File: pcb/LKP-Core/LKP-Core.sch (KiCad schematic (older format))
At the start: 30 parts, among them J1 Intercon L, J2 Intercon R, J3 Power JST XH, J4 IO, J5 SWD, U1 CY8C4246AZI-M445

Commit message: Initial placement plan
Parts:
- C1, C10, C4, C6: footprint (none) -> Capacitor_SMD:C_0603_1608Metric; Comments (none) -> Jellybean part. X5R or better.; Part Number (none) -> CL10B104KA8NNNC
- C11, C2, C3, C5, C8: footprint (none) -> Capacitor_SMD:C_0603_1608Metric; Comments (none) -> Jellybean part. X5R or better.; Part Number (none) -> CC0603KRX5R8BB105
- C7: value 10nF -> 10nF C0G; footprint (none) -> Capacitor_SMD:C_0805_2012Metric; Manufacturer (none) -> Murata Electronics; Part Number (none) -> GRM2195C1H103JA01D; Supplier (none) -> lcsc:C97905
- C9: value 2.2nF -> 2.2nF C0G; footprint (none) -> Capacitor_SMD:C_0603_1608Metric; Manufacturer (none) -> Murata Electronics; Part Number (none) -> GCM1885C1H222JA16D; Supplier (none) -> lcsc:C343869
- D1: value LED -> Yellow; footprint (none) -> LED_SMD:LED_0805_2012Metric
- D2: footprint (none) -> Diode_SMD:D_SOD-123; Part Number (none) -> MBR0520L
- FB1: footprint (none) -> Inductor_SMD:L_0603_1608Metric
- J1, J2: footprint (none) -> Connector_PinSocket_2.54mm:PinSocket_2x09_P2.54mm_Vertical_SMD
- J3: value Power JST XH -> Power JST PH; footprint (none) -> Connector_JST:JST_PH_S2B-PH-SM4-TB_1x02-1MP_P2.00mm_Horizontal; Comments (none) -> Jellybean part.
- J4: footprint (none) -> Connector_PinHeader_2.54mm:PinHeader_1x06_P2.54mm_Vertical
- J5: footprint (none) -> Connector_PinHeader_2.54mm:PinHeader_1x05_P2.54mm_Vertical
- R1, R2: footprint (none) -> Resistor_SMD:R_0603_1608Metric
- RN1: footprint (none) -> Resistor_SMD:R_Array_Convex_4x0402; Manufacturer (none) -> Uniroyal; Part Number (none) -> 4D02WGJ0561TCE; Supplier (none) -> lcsc:C270386
- RN2, RN3, RN4, RN5, RN6, RN7, RN8: footprint (none) -> Resistor_SMD:R_Array_Convex_4x0402; Part Number (none) -> 4D02WGJ0561TCE
- U1: Part Number (none) -> CY8C4246AZI-M445
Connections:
- wire segments 171 -> 176
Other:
- moved on the sheet: C9, D2, FB1

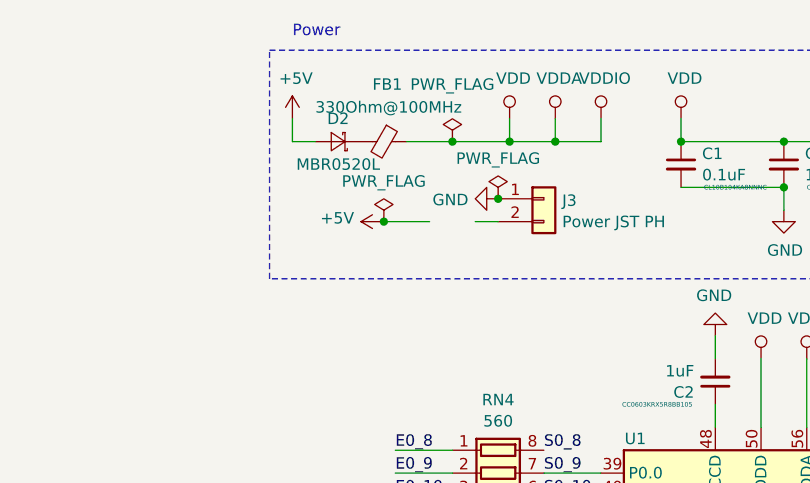
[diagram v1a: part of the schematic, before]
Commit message: Define net classes
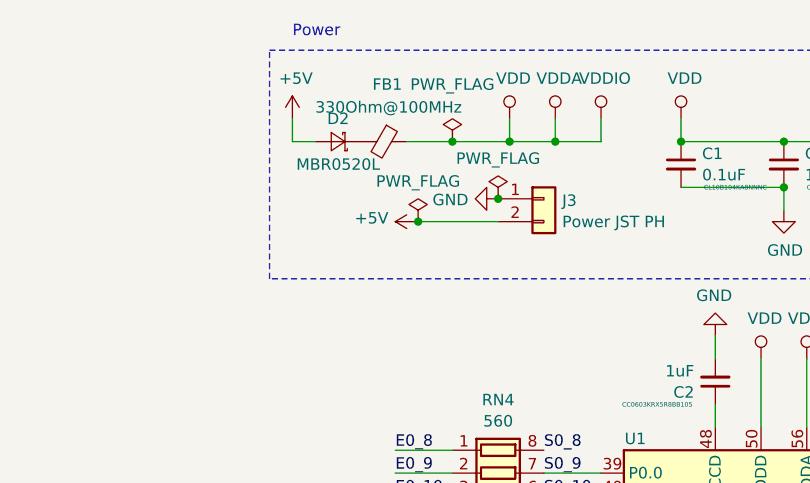
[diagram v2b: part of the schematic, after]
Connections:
- wire segments 176 -> 175
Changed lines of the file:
@@
 L power:+5V #PWR02
 U 1 1 5D5A13B9
-P 3900 1400
-F 0 "#PWR02" H 3900 1250 50  0001 C CNN
-F 1 "+5V" V 3915 1530 50  0000 L CNN
-F 2 "" H 3900 1400 50  0001 C CNN
-F 3 "" H 3900 1400 50  0001 C CNN
-	1    3900 1400
+P 4050 1400
+F 0 "#PWR02" H 4050 1250 50  0001 C CNN
+F 1 "+5V" V 4065 1530 50  0000 L CNN
+F 2 "" H 4050 1400 50  0001 C CNN
+F 3 "" H 4050 1400 50  0001 C CNN
+	1    4050 1400
 	0    -1   -1   0
 $EndComp
@@
 L power:PWR_FLAG #FLG01
 U 1 1 5D770DDD
-P 3900 1400
-F 0 "#FLG01" H 3900 1475 50  0001 C CNN
-F 1 "PWR_FLAG" H 3900 1576 50  0000 C CNN
-F 2 "" H 3900 1400 50  0001 C CNN
-F 3 "~" H 3900 1400 50  0001 C CNN
-	1    3900 1400
+P 4050 1400
+F 0 "#FLG01" H 4050 1475 50  0001 C CNN
+F 1 "PWR_FLAG" H 4050 1576 50  0000 C CNN
+F 2 "" H 4050 1400 50  0001 C CNN
+F 3 "~" H 4050 1400 50  0001 C CNN
+	1    4050 1400
 	1    0    0    -1
 $EndComp
@@
 	-1   0    0    1
 $EndComp
-Wire Wire Line
-	4400 1400 4300 1400
-Connection ~ 3900 1400
-Wire Wire Line
-	3900 1400 4100 1400
 Wire Wire Line
 	6450 3600 7700 3600
@@
 Wire Wire Line
 	3600 1050 3500 1050
+Wire Wire Line
+	4400 1400 4050 1400
+Connection ~ 4050 1400
 $EndSCHEMATC

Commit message: Finishing up
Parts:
- removed D1: Yellow, LED_SMD:LED_0805_2012Metric, symbol Device:LED
- removed R1: 1k, Resistor_SMD:R_0603_1608Metric, symbol Device:R_Small
- renumbered D2 to D1
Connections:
- net labels removed: LED_STAT
- wire segments 175 -> 172
- no-connect marks 8 -> 9
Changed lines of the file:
@@
 Text Label 7200 2600 2    50   ~ 0
 LED
-Text Label 4450 4000 0    50   ~ 0
-LED_STAT
 Wire Wire Line
 	6700 3200 6450 3200
@@
 Wire Wire Line
 	4000 3100 4850 3100
-$Comp
-L Device:LED D1
-U 1 1 5D6D02DC
-P 3700 4150
-F 0 "D1" H 3693 4369 50  0000 C CNN
-F 1 "Yellow" H 3693 4276 50  0000 C CNN
-F 2 "LED_SMD:LED_0805_2012Metric" H 3700 4150 50  0001 C CNN
-F 3 "~" H 3700 4150 50  0001 C CNN
-	1    3700 4150
-	1    0    0    -1
-$EndComp
-Wire Wire Line
-	4200 4000 4200 4150
-Wire Wire Line
-	4200 4000 4850 4000
-$Comp
-L power:GND #PWR01
-U 1 1 5D6DFC49
-P 3550 4150
-F 0 "#PWR01" H 3550 3900 50  0001 C CNN
-F 1 "GND" V 3555 4020 50  0000 R CNN
-F 2 "" H 3550 4150 50  0001 C CNN
-F 3 "" H 3550 4150 50  0001 C CNN
-	1    3550 4150
-	0    1    1    0
-$EndComp
-$Comp
-L Device:R_Small R1
-U 1 1 5D6ECD34
-P 3950 4150
-F 0 "R1" V 3751 4150 50  0000 C CNN
-F 1 "1k" V 3844 4150 50  0000 C CNN
-F 2 "Resistor_SMD:R_0603_1608Metric" H 3950 4150 50  0001 C CNN
-F 3 "~" H 3950 4150 50  0001 C CNN
-	1    3950 4150
-	0    1    1    0
-$EndComp
-Wire Wire Line
-	4050 4150 4200 4150
 Wire Wire Line
 	3500 950  3500 1050
@@
 Sensor Interconnects
 Wire Notes Line
-	8200 3350 10050 3350
-Wire Notes Line
 	10050 3350 10050 4150
 Wire Notes Line
@@
 I/O
 $Comp
-L Device:D_Schottky_Small D2
+L Device:D_Schottky_Small D1
 U 1 1 5D93FA0B
 P 3700 1050
-F 0 "D2" H 3700 950 50  0000 C CNN
+F 0 "D1" H 3700 950 50  0000 C CNN
 F 1 "MBR0520L" H 3700 1150 50  0000 C CNN
 F 2 "Diode_SMD:D_SOD-123" V 3700 1050 50  0001 C CNN
@@
 	4400 1400 4050 1400
 Connection ~ 4050 1400
+NoConn ~ 4850 4000
 $EndSCHEMATC

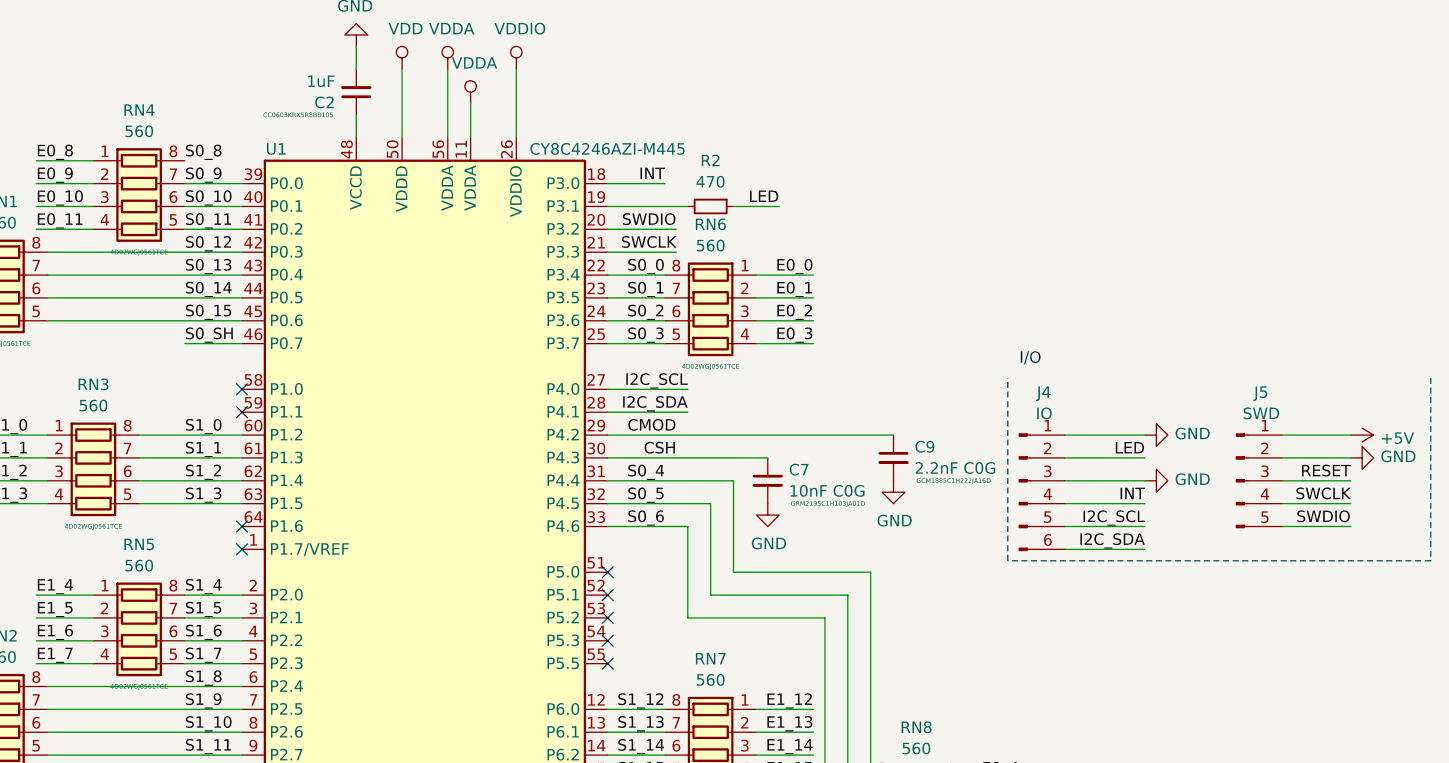
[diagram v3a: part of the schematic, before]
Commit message: Move various IO pins down
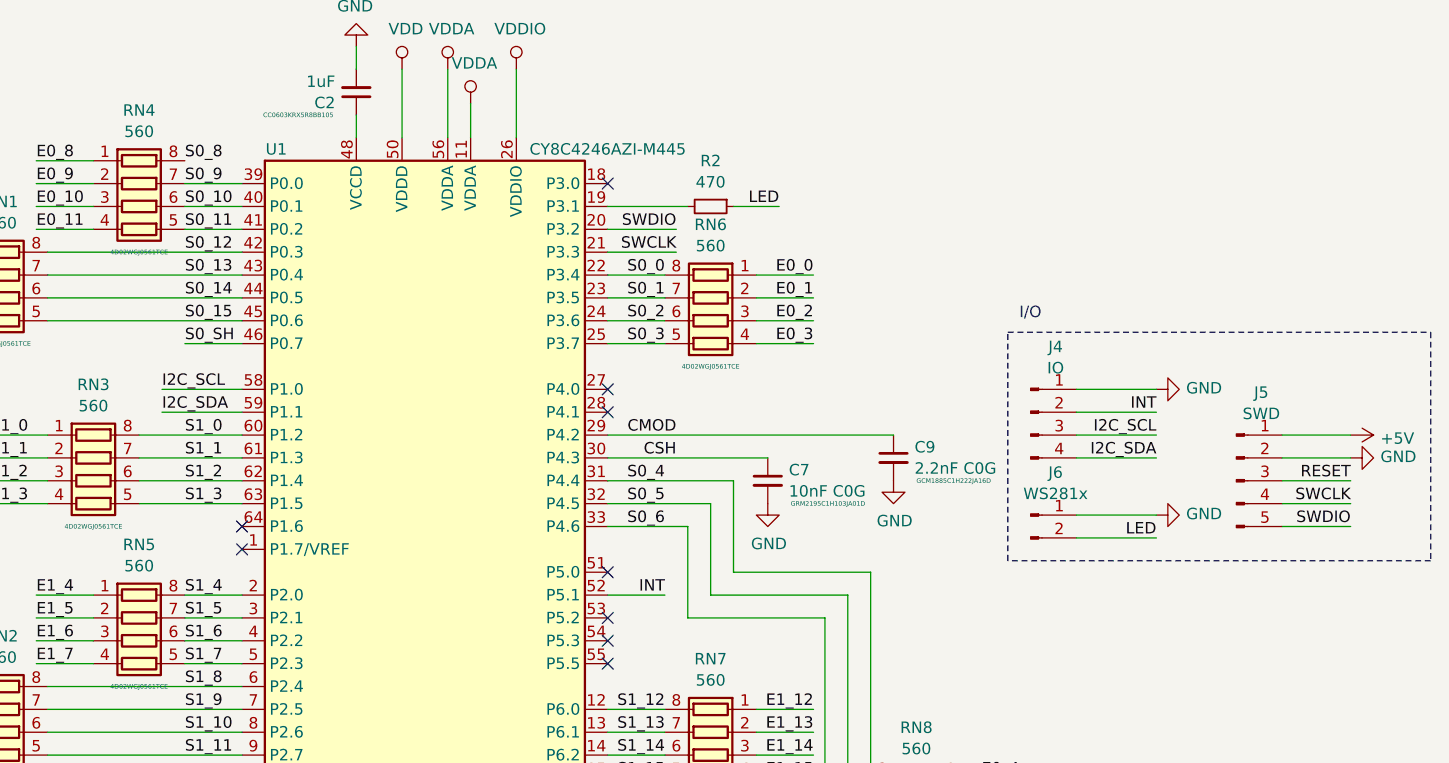
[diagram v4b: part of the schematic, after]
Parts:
- removed J4: IO, Connector_PinHeader_2.54mm:PinHeader_1x06_P2.54mm_Vertical, symbol Connector:Conn_01x06_Male
- added J4: IO, symbol Connector:Conn_01x04_Male
- added J6: WS281x, symbol Connector:Conn_01x02_Male
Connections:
- net GND: now also J4.1 (Pin_1), J6.1 (Pin_1)
- net I2C_SCL: now also U1.58 (P1.0), J4.3 (Pin_3); no longer U1.27 (P4.0)
- net I2C_SDA: now also U1.59 (P1.1), J4.4 (Pin_4); no longer U1.28 (P4.1)
- net INT: now also U1.52 (P5.1), J4.2 (Pin_2); no longer U1.18 (P3.0)
- net LED: now also J6.2 (Pin_2)
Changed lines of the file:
@@
 	0    1    1    0
 $EndComp
-Wire Wire Line
-	6450 3500 6800 3500
-Wire Wire Line
-	6800 3400 6450 3400
-Text Label 6800 3500 2    50   ~ 0
+Text Label 4500 3500 0    50   ~ 0
 I2C_SDA
-Text Label 6800 3400 2    50   ~ 0
+Text Label 4500 3400 0    50   ~ 0
 I2C_SCL
-NoConn ~ 4850 3500
-NoConn ~ 4850 3400
 NoConn ~ 6450 4600
 NoConn ~ 6450 4500
 NoConn ~ 6450 4400
-NoConn ~ 6450 4300
 NoConn ~ 6450 4200
 Wire Wire Line
@@
 	0    -1   1    0
 $EndComp
-Wire Wire Line
-	6700 2500 6450 2500
-Text Label 6700 2500 2    50   ~ 0
+Text Label 6700 4300 2    50   ~ 0
 INT
 Text Label 7200 2600 2    50   ~ 0
@@
 L power:GND #PWR021
 U 1 1 5D7937F4
-P 8800 3600
-F 0 "#PWR021" H 8800 3350 50  0001 C CNN
-F 1 "GND" V 8805 3470 50  0000 R CNN
-F 2 "" H 8800 3600 50  0001 C CNN
-F 3 "" H 8800 3600 50  0001 C CNN
-	1    8800 3600
+P 8850 3950
+F 0 "#PWR021" H 8850 3700 50  0001 C CNN
+F 1 "GND" V 8855 3820 50  0000 R CNN
+F 2 "" H 8850 3950 50  0001 C CNN
+F 3 "" H 8850 3950 50  0001 C CNN
+	1    8850 3950
 	0    -1   -1   0
 $EndComp
-Text Label 8800 4000 2    50   ~ 0
+Text Label 8850 3600 2    50   ~ 0
 I2C_SCL
 Wire Wire Line
-	8800 3600 8450 3600
-Wire Wire Line
-	8800 4000 8450 4000
-Text Label 8800 4100 2    50   ~ 0
+	8850 3600 8500 3600
+Text Label 8850 3700 2    50   ~ 0
 I2C_SDA
 Wire Wire Line
-	8800 4100 8450 4100
+	8850 3700 8500 3700
 $Comp
 L power:GND #PWR022
 U 1 1 5D7B99DC
-P 8800 3800
-F 0 "#PWR022" H 8800 3550 50  0001 C CNN
-F 1 "GND" V 8805 3670 50  0000 R CNN
-F 2 "" H 8800 3800 50  0001 C CNN
-F 3 "" H 8800 3800 50  0001 C CNN
-	1    8800 3800
+P 8850 3400
+F 0 "#PWR022" H 8850 3150 50  0001 C CNN
+F 1 "GND" V 8855 3270 50  0000 R CNN
+F 2 "" H 8850 3400 50  0001 C CNN
+F 3 "" H 8850 3400 50  0001 C CNN
+	1    8850 3400
 	0    -1   -1   0
 $EndComp
-$Comp
-L Connector:Conn_01x06_Male J4
-U 1 1 5D7BAAC8
-P 8250 3800
-F 0 "J4" H 8359 4186 50  0000 C CNN
-F 1 "IO" H 8359 4093 50  0000 C CNN
-F 2 "Connector_PinHeader_2.54mm:PinHeader_1x06_P2.54mm_Vertical" H 8250 3800 50  0001 C CNN
-F 3 "~" H 8250 3800 50  0001 C CNN
-	1    8250 3800
-	1    0    0    -1
-$EndComp
-Text Label 8800 3900 2    50   ~ 0
+Text Label 8850 3500 2    50   ~ 0
 INT
 Wire Wire Line
-	8450 3900 8800 3900
-Wire Wire Line
-	8800 3800 8450 3800
-Text Label 8800 3700 2    50   ~ 0
+	8500 3500 8850 3500
+Wire Wire Line
+	8850 3400 8500 3400
+Text Label 8850 4050 2    50   ~ 0
 LED
-Wire Wire Line
-	8800 3700 8450 3700
 $Comp
 L Device:R_Small R2
@@
 Sensor Interconnects
 Wire Notes Line
-	10050 3350 10050 4150
-Wire Notes Line
 	10050 4150 8200 4150
-Wire Notes Line
-	8200 4150 8200 3350
-Text Notes 8250 3300 0    50   ~ 0
+Text Notes 8250 3100 0    50   ~ 0
 I/O
 $Comp
@@
 Connection ~ 4050 1400
 NoConn ~ 4850 4000
+Wire Wire Line
+	6700 4300 6450 4300
+Wire Wire Line
+	4500 3400 4850 3400
+Wire Wire Line
+	4850 3500 4500 3500
+NoConn ~ 6450 3500
+NoConn ~ 6450 3400
+NoConn ~ 6450 2500
+$Comp
+L Connector:Conn_01x04_Male J4
+U 1 1 5D5044ED
+P 8300 3500
+F 0 "J4" H 8409 3786 50  0000 C CNN
+F 1 "IO" H 8409 3693 50  0000 C CNN
+F 2 "" H 8300 3500 50  0001 C CNN
+F 3 "~" H 8300 3500 50  0001 C CNN
+	1    8300 3500
+	1    0    0    -1
+$EndComp
+$Comp
+L Connector:Conn_01x02_Male J6
+U 1 1 5D520F05
+P 8300 3950
+F 0 "J6" H 8409 4136 50  0000 C CNN
+F 1 "WS281x" H 8409 4043 50  0000 C CNN
+F 2 "" H 8300 3950 50  0001 C CNN
+F 3 "~" H 8300 3950 50  0001 C CNN
+	1    8300 3950
+	1    0    0    -1
+$EndComp
+Wire Wire Line
+	8850 3950 8500 3950
+Wire Wire Line
+	8500 4050 8850 4050
+Wire Notes Line
+	8200 4150 8200 3150
+Wire Notes Line
+	8200 3150 10050 3150
+Wire Notes Line
+	10050 3150 10050 4150
 $EndSCHEMATC

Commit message: Apply changes
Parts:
- J4: footprint (none) -> Connector_PinHeader_2.54mm:PinHeader_1x04_P2.54mm_Vertical
- J6: footprint (none) -> Connector_PinHeader_2.54mm:PinHeader_1x02_P2.54mm_Vertical
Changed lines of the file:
@@
 F 0 "J4" H 8409 3786 50  0000 C CNN
 F 1 "IO" H 8409 3693 50  0000 C CNN
-F 2 "" H 8300 3500 50  0001 C CNN
+F 2 "Connector_PinHeader_2.54mm:PinHeader_1x04_P2.54mm_Vertical" H 8300 3500 50  0001 C CNN
 F 3 "~" H 8300 3500 50  0001 C CNN
 	1    8300 3500
@@
 F 0 "J6" H 8409 4136 50  0000 C CNN
 F 1 "WS281x" H 8409 4043 50  0000 C CNN
-F 2 "" H 8300 3950 50  0001 C CNN
+F 2 "Connector_PinHeader_2.54mm:PinHeader_1x02_P2.54mm_Vertical" H 8300 3950 50  0001 C CNN
 F 3 "~" H 8300 3950 50  0001 C CNN
 	1    8300 3950

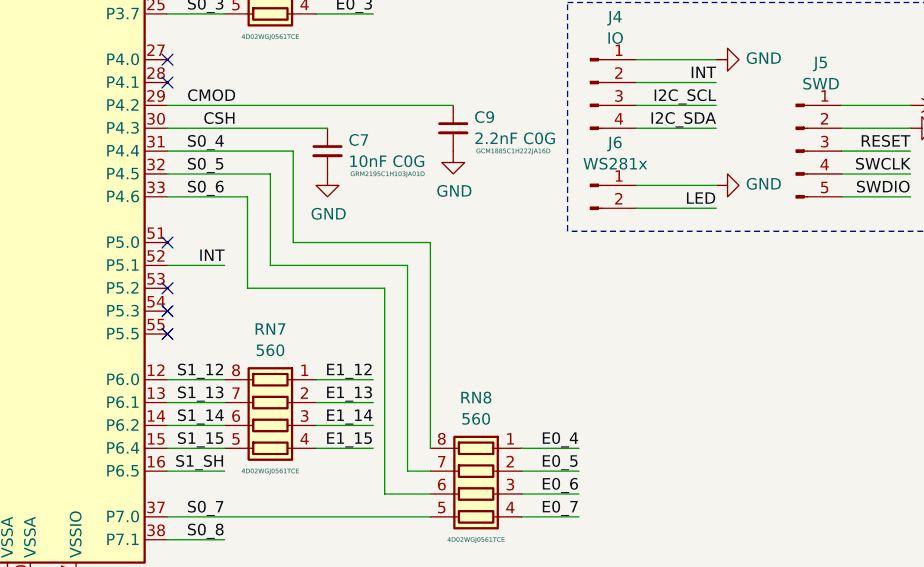
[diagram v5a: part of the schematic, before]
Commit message: Add the status LED back
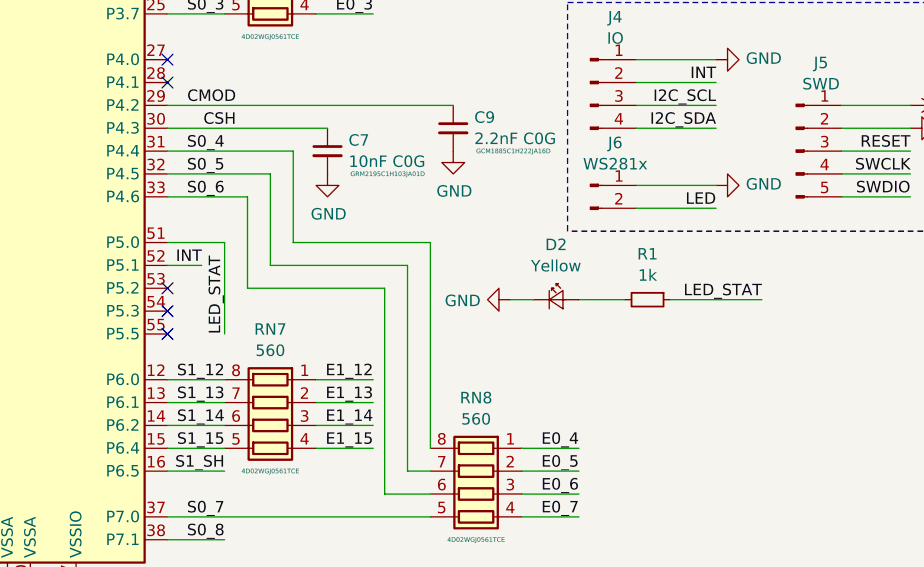
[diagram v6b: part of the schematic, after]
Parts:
- added D2: Yellow, LED_SMD:LED_0805_2012Metric, symbol Device:LED_Small
- added R1: 1k, Resistor_SMD:R_0603_1608Metric, symbol Device:R_Small
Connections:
- net GND: now also D2.1 (K)
- net LED_STAT: now reaches U1.51 (P5.0)
- net LED_STAT: now also R1.1
- new net: D2.2 (A), R1.2
- no-connect marks 9 -> 8
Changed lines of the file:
@@
 NoConn ~ 6450 4500
 NoConn ~ 6450 4400
-NoConn ~ 6450 4200
 Wire Wire Line
 	6700 5500 6450 5500
@@
 	0    -1   1    0
 $EndComp
-Text Label 6700 4300 2    50   ~ 0
+Text Label 6600 4300 2    50   ~ 0
 INT
 Text Label 7200 2600 2    50   ~ 0
@@
 NoConn ~ 4850 4000
 Wire Wire Line
-	6700 4300 6450 4300
-Wire Wire Line
 	4500 3400 4850 3400
 Wire Wire Line
@@
 Wire Notes Line
 	10050 3150 10050 4150
+Wire Wire Line
+	6450 4200 6700 4200
+Wire Wire Line
+	6450 4300 6600 4300
+Text Label 6700 4600 1    50   ~ 0
+LED_STAT
+Wire Wire Line
+	6700 4200 6700 4600
+Text Label 9050 4450 2    50   ~ 0
+LED_STAT
+$Comp
+L Device:R_Small R1
+U 1 1 5D57FBCF
+P 8550 4450
+F 0 "R1" V 8351 4450 50  0000 C CNN
+F 1 "1k" V 8444 4450 50  0000 C CNN
+F 2 "Resistor_SMD:R_0603_1608Metric" H 8550 4450 50  0001 C CNN
+F 3 "~" H 8550 4450 50  0001 C CNN
+	1    8550 4450
+	0    1    1    0
+$EndComp
+Wire Wire Line
+	8650 4450 9050 4450
+Wire Wire Line
+	8450 4450 8250 4450
+$Comp
+L power:GND #PWR0104
+U 1 1 5D59BA60
+P 7950 4450
+F 0 "#PWR0104" H 7950 4200 50  0001 C CNN
+F 1 "GND" V 7955 4320 50  0000 R CNN
+F 2 "" H 7950 4450 50  0001 C CNN
+F 3 "" H 7950 4450 50  0001 C CNN
+	1    7950 4450
+	0    1    1    0
+$EndComp
+Wire Wire Line
+	8050 4450 7950 4450
+$Comp
+L Device:LED_Small D2
+U 1 1 5D57DFAF
+P 8150 4450
+F 0 "D2" H 8150 4690 50  0000 C CNN
+F 1 "Yellow" H 8150 4597 50  0000 C CNN
+F 2 "LED_SMD:LED_0805_2012Metric" V 8150 4450 50  0001 C CNN
+F 3 "~" V 8150 4450 50  0001 C CNN
+	1    8150 4450
+	1    0    0    -1
+$EndComp
 $EndSCHEMATC
